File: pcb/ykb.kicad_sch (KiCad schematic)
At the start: 90 parts, among them J1 Conn_01x08_Socket, U1 Helios

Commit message: all done other than mounting holes :3
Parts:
- J1: value Conn_01x08_Socket -> Conn_01x07_Socket; footprint Connector_PinHeader_2.54mm:PinHeader_1x08_P2.54mm_Vertical -> Connector_PinHeader_2.54mm:PinHeader_1x07_P2.54mm_Vertical
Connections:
- net DBL: no longer names the net of U1.34 (P25)
- net DBL: no longer J1.8 (BL)
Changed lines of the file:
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@@
 	(wire
 		(pts
-			(xy 143.51 100.33) (xy 143.51 106.68)
-		)
-		(stroke
-			(width 0)
-			(type default)
-		)
-	)
-	(wire
-		(pts
 			(xy 102.87 69.85) (xy 102.87 88.9)
 		)
@@
 		)
 	)
-	(global_label "DBL"
-		(shape input)
-		(at 143.51 106.68 270)
-		(fields_autoplaced yes)
-		(effects
-			(font
-				(size 1.27 1.27)
-			)
-			(justify right)
-		)
-		(property "Intersheetrefs" "${INTERSHEET_REFS}"
-			(at 143.51 113.2333 90)
-			(effects
-				(font
-					(size 1.27 1.27)
-				)
-				(justify right)
-				(hide yes)
-			)
-		)
-	)
 	(global_label "col 2"
 		(shape input)
@@
 		)
 	)
-	(global_label "DBL"
-		(shape input)
-		(at 139.7 55.88 180)
-		(fields_autoplaced yes)
-		(effects
-			(font
-				(size 1.27 1.27)
-			)
-			(justify right)
-		)
-		(property "Intersheetrefs" "${INTERSHEET_REFS}"
-			(at 133.1467 55.88 0)
-			(effects
-				(font
-					(size 1.27 1.27)
-				)
-				(justify right)
-				(hide yes)
-			)
-		)
-	)
 	(global_label "col 10"
 		(shape input)
@@
 			)
 		)
-		(property "Value" "Conn_01x08_Socket"
+		(property "Value" "Conn_01x07_Socket"
 			(at 152.4 95.25 0)
 			(effects
@@
 			)
 		)
-		(property "Footprint" "Connector_PinHeader_2.54mm:PinHeader_1x08_P2.54mm_Vertical"
+		(property "Footprint" "Connector_PinHeader_2.54mm:PinHeader_1x07_P2.54mm_Vertical"
 			(at 147.32 100.33 0)
 			(effects
@@
 			)
 		)
-		(property "Description" "Generic connector, single row, 01x08, script generated"
+		(property "Description" "Generic connector, single row, 01x07, script generated"
 			(at 147.32 100.33 0)
 			(effects

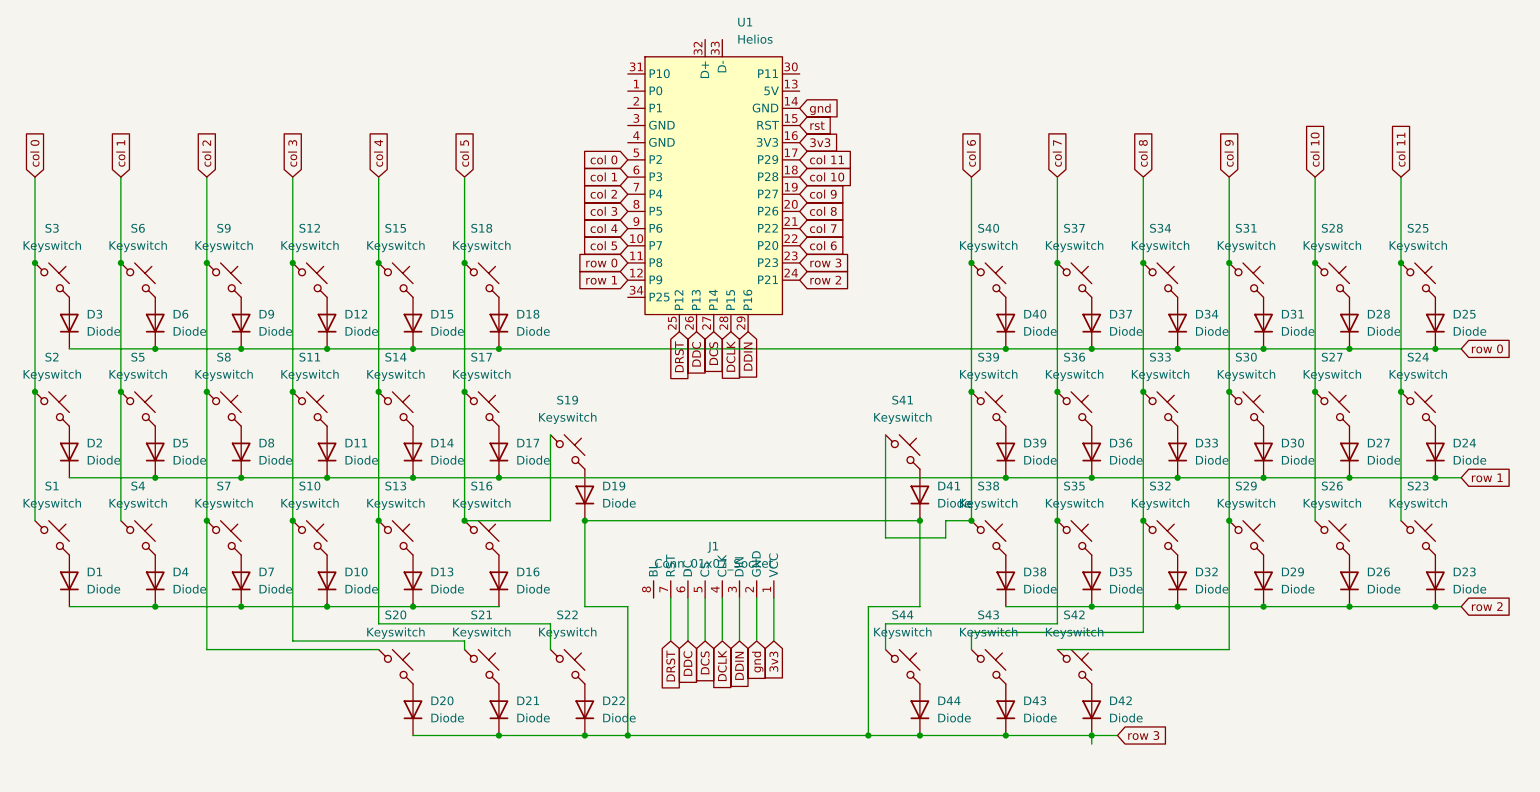
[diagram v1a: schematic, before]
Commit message: fixed lcd and some design rule errors
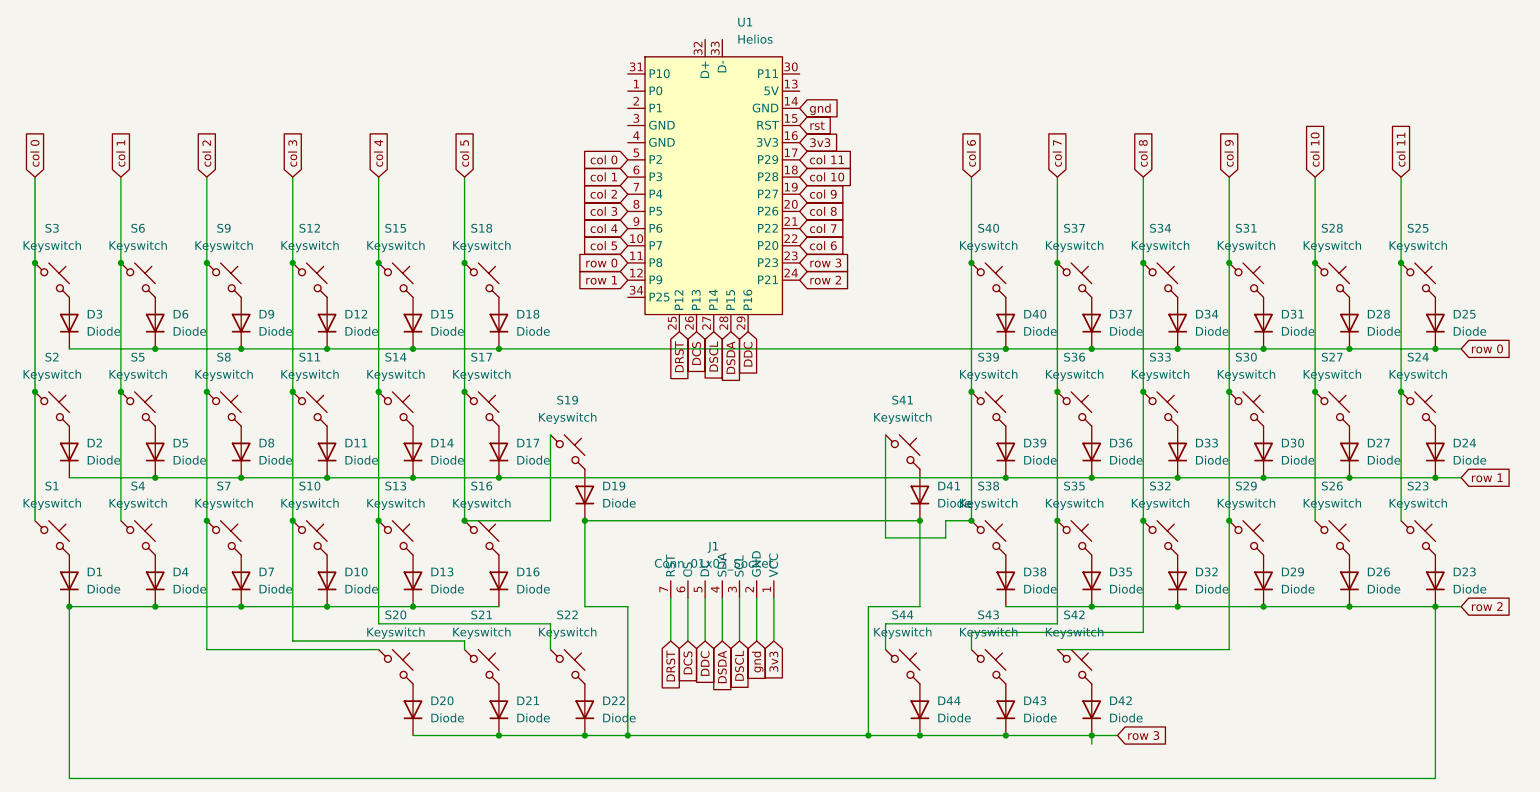
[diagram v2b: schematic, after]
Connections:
- net DCS: now also J1.6 (CS), U1.26 (P13); no longer J1.5 (CS), U1.27 (P14)
- net DDC: now also J1.5 (DC), U1.29 (P16); no longer J1.6 (DC), U1.26 (P13)
- net row 2: now also D1.1 (K), D10.1 (K), D13.1 (K), D16.1 (K), D4.1 (K), D7.1 (K)
- net DCLK renamed DSDA
- net DDIN renamed DSCL
- net DSCL: now also U1.27 (P14); no longer U1.29 (P16)
